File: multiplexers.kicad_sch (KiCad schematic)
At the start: 12 parts, among them U2 74HC4067, U3 74HC4067, U4 74HC4067, U5 74HC4067, U7 74HC4067, U8 74HC4067

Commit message: dip switch
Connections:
- net KEYS_0_12: now also U8.5 (I4); no longer U8.7 (I2)
- net KEYS_1_13: now also U8.3 (I6); no longer U8.5 (I4)
- net KEYS_2_12: now also U8.4 (I5); no longer U8.3 (I6)

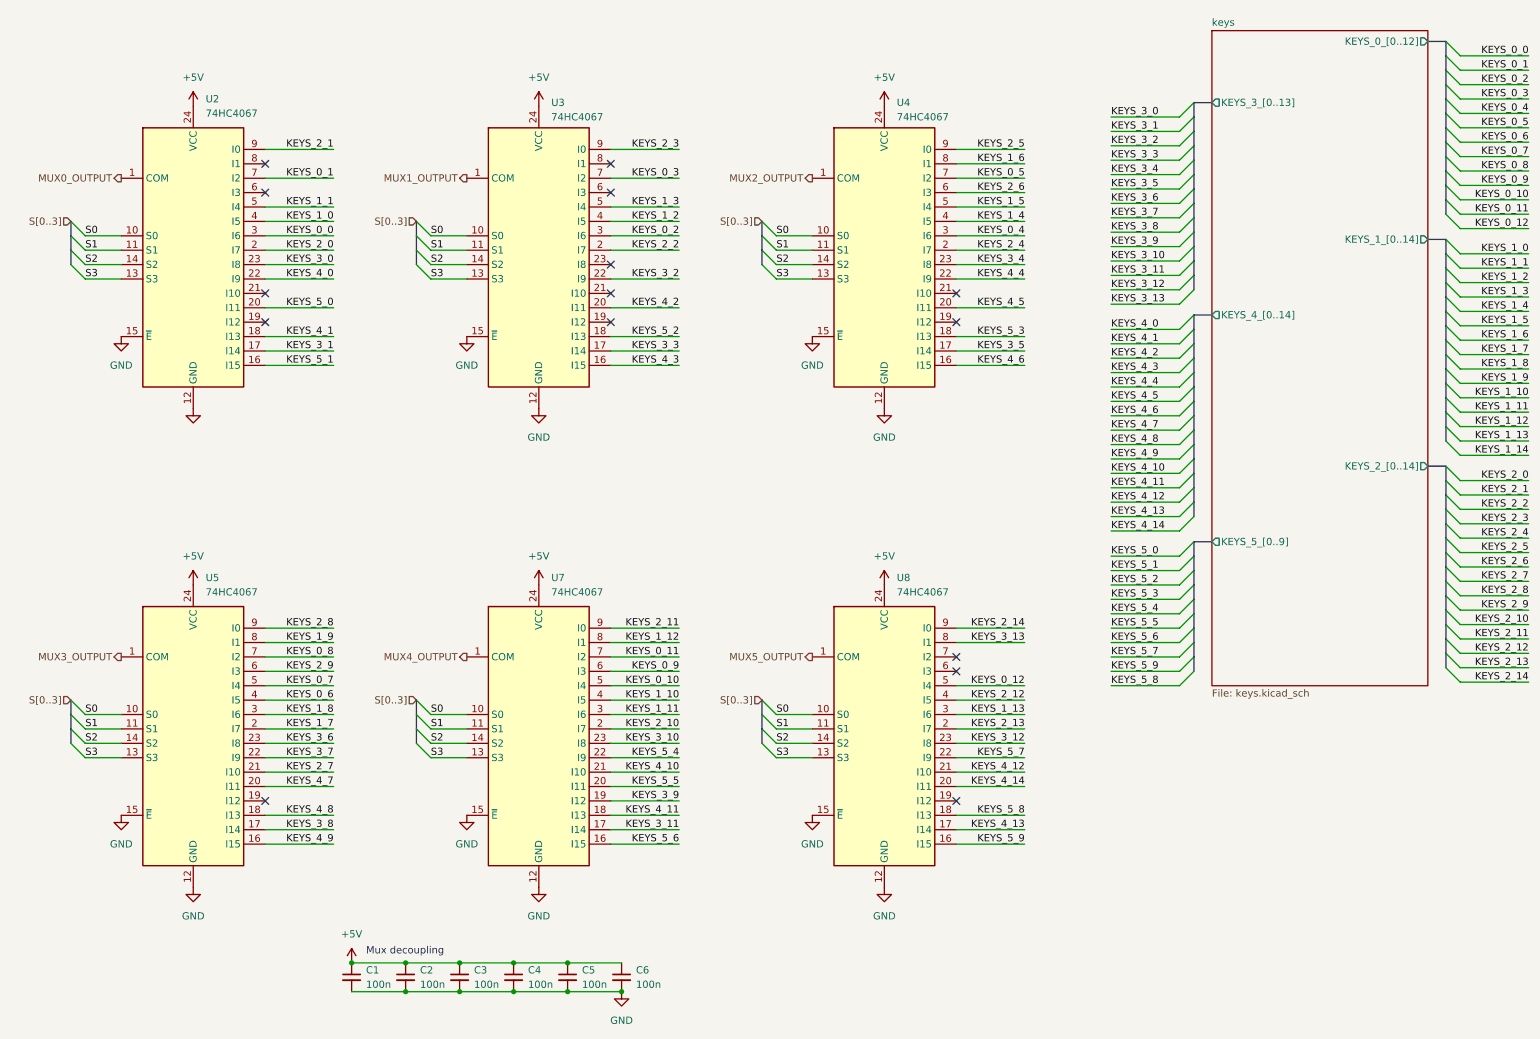
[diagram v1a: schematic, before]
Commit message: add 0R usb termination resistors change muxes to 3V3
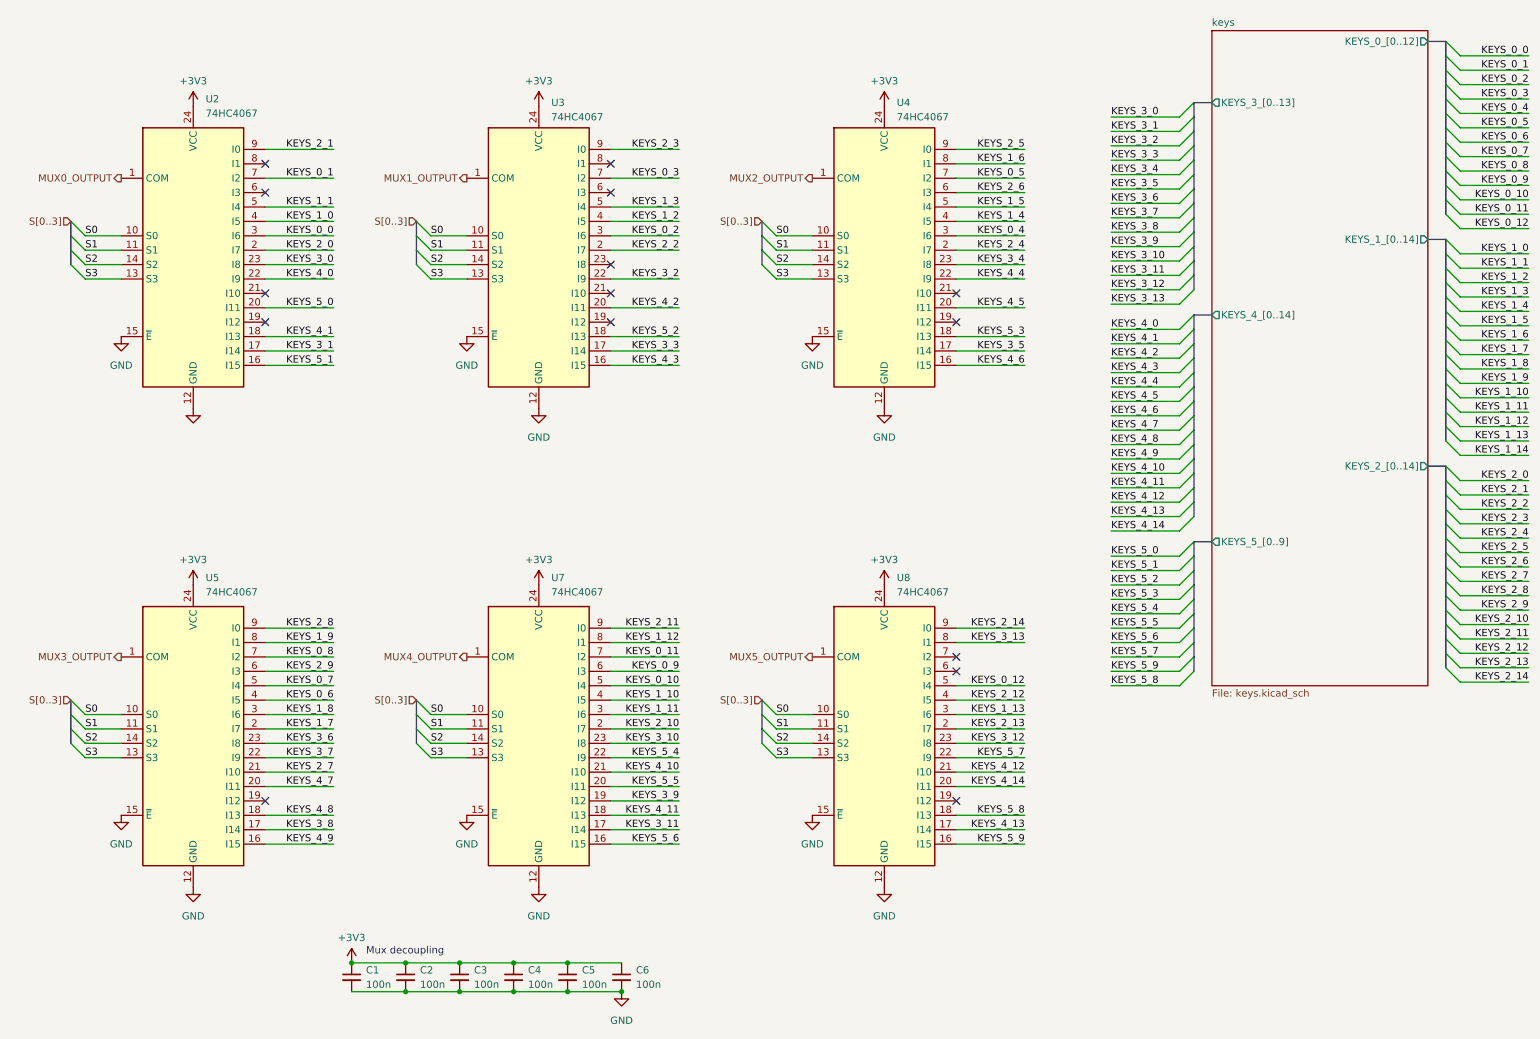
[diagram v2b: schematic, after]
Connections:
- net +5V renamed +3V3

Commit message: update to kicad 8
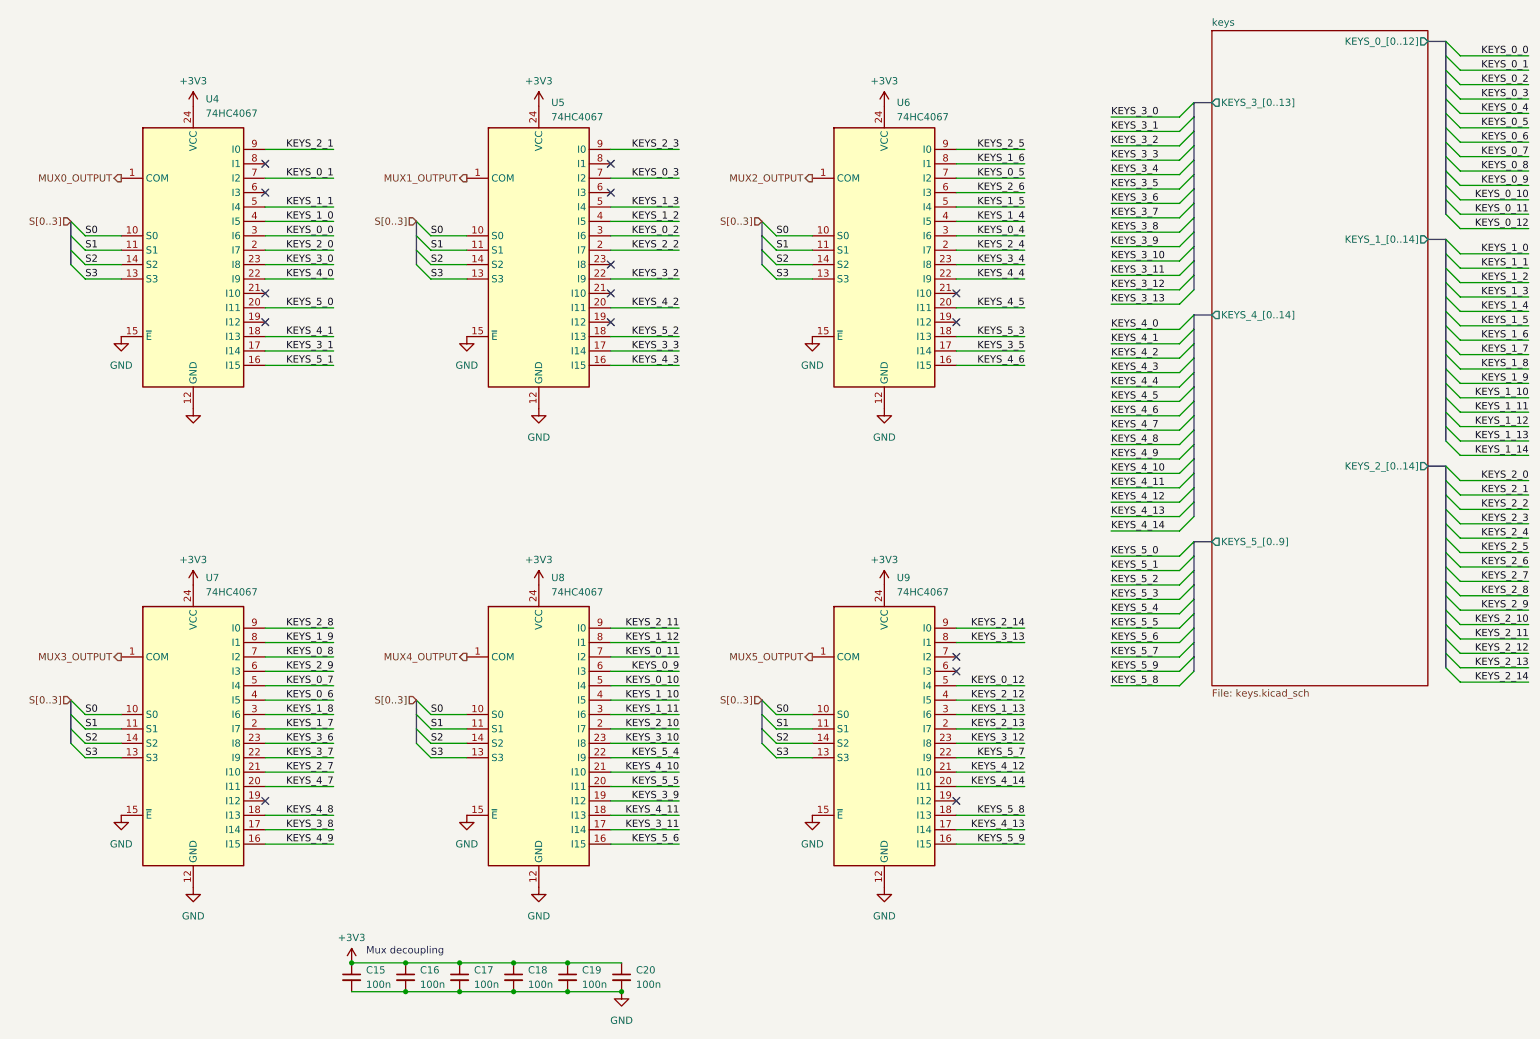
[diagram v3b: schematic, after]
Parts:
- renumbered C1 to C15, C2 to C16, C3 to C17, C4 to C18, C5 to C19, C6 to C20, U2 to U4, U3 to U5, U4 to U6, U5 to U7, U7 to U8, U8 to U9
